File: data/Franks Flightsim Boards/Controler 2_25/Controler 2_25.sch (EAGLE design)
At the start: 16 parts, among them IC1 3_3V, IC2 5V, J3 External, J4 FEMALE 2x3

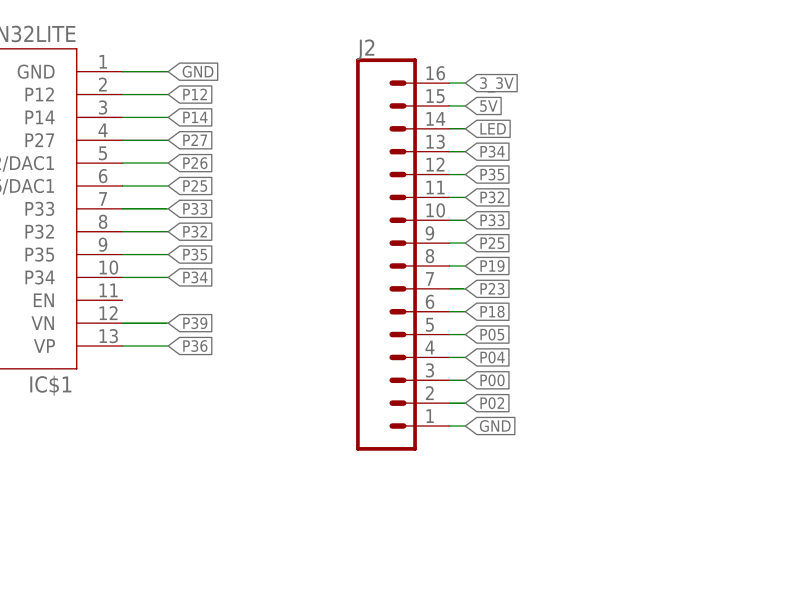
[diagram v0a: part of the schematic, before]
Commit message: new PCB
Updated with new pcb for 2_25 version
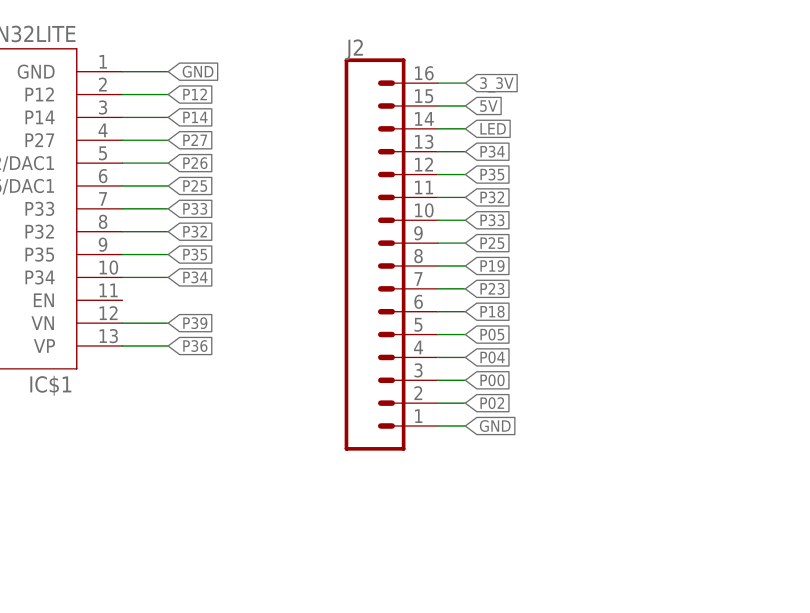
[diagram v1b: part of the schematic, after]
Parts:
- J2: device SparkFun-Connectors:CONN_16CENTER -> SparkFun-Connectors:CONN_16
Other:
- moved on the sheet: J2

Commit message: Update dev status
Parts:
- C1: device resistor:C-EUC0805 -> resistor:C-EUC1206
- C5: device resistor:CPOL-EU153CLV-0505 -> resistor:CPOL-EU153CLV-0605
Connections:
- net P12 renamed SRV1
- removed net P13: IC$1.P13/R14, J4.1
- removed net P15: IC$1.P15/R13, J4.2
- new net SRV2: IC$1.P15/R13, J4.1
- new net SRV3: IC$1.P13/R14, J4.2
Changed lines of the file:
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@@
 </class>
 <class number="1" name="GND" width="0.508" drill="0">
+<clearance class="1" value="0.254"/>
 </class>
 <class number="2" name="12V" width="0.762" drill="0">
@@
 <part name="IC2" library="SparkFun-IC-Power" library_urn="urn:adsk.eagle:library:526" deviceset="V_REG_LM1117" device="SOT223" package3d_urn="urn:adsk.eagle:package:39069/1" value="5V"/>
 <part name="C2" library="resistor" library_urn="urn:adsk.eagle:library:348" deviceset="CPOL-EU" device="CT3528" package3d_urn="urn:adsk.eagle:package:25815/1" value="47uF"/>
-<part name="C1" library="resistor" library_urn="urn:adsk.eagle:library:348" deviceset="C-EU" device="C0805" package3d_urn="urn:adsk.eagle:package:26137/1" value="100nF"/>
+<part name="C1" library="resistor" library_urn="urn:adsk.eagle:library:348" deviceset="C-EU" device="C1206" package3d_urn="urn:adsk.eagle:package:26140/1" value="100nF"/>
 <part name="C4" library="resistor" library_urn="urn:adsk.eagle:library:348" deviceset="CPOL-EU" device="CT3528" package3d_urn="urn:adsk.eagle:package:25815/1" value="47uF"/>
 <part name="C3" library="resistor" library_urn="urn:adsk.eagle:library:348" deviceset="C-EU" device="C0805" package3d_urn="urn:adsk.eagle:package:26137/1" value="100nF"/>
@@
 <part name="J1" library="SparkFun-Connectors" library_urn="urn:adsk.eagle:library:513" deviceset="CONN_03" device="" package3d_urn="urn:adsk.eagle:package:38063/1"/>
 <part name="J4" library="SparkFun-Connectors" library_urn="urn:adsk.eagle:library:513" deviceset="CONN_03X2" device="FEMALE" package3d_urn="urn:adsk.eagle:package:38016/1" value="FEMALE 2x3"/>
-<part name="C5" library="resistor" library_urn="urn:adsk.eagle:library:348" deviceset="CPOL-EU" device="153CLV-0505" package3d_urn="urn:adsk.eagle:package:25890/1" value="47uF"/>
+<part name="C5" library="resistor" library_urn="urn:adsk.eagle:library:348" deviceset="CPOL-EU" device="153CLV-0605" package3d_urn="urn:adsk.eagle:package:25889/1" value="47uF"/>
 <part name="C6" library="resistor" library_urn="urn:adsk.eagle:library:348" deviceset="C-EU" device="C0805" package3d_urn="urn:adsk.eagle:package:26137/1" value="100nF"/>
 </parts>
@@
 </segment>
 </net>
-<net name="P15" class="0">
+<net name="SRV3" class="0">
+<segment>
+<pinref part="IC$1" gate="G$1" pin="P13/R14"/>
+<wire x1="38.1" y1="106.68" x2="33.02" y2="106.68" width="0.1524" layer="91"/>
+<label x="33.02" y="106.68" size="1.27" layer="95" ratio="7" rot="R180" xref="yes"/>
+</segment>
+<segment>
+<pinref part="J4" gate="G$1" pin="2"/>
+<wire x1="7.62" y1="58.42" x2="10.16" y2="58.42" width="0.1524" layer="91"/>
+<label x="10.16" y="58.42" size="1.27" layer="95" xref="yes"/>
+</segment>
+</net>
+<net name="SRV2" class="0">
 <segment>
 <pinref part="IC$1" gate="G$1" pin="P15/R13"/>
@@
 </segment>
 <segment>
-<pinref part="J4" gate="G$1" pin="2"/>
-<wire x1="7.62" y1="58.42" x2="10.16" y2="58.42" width="0.1524" layer="91"/>
-<label x="10.16" y="58.42" size="1.27" layer="95" xref="yes"/>
-</segment>
-</net>
-<net name="P13" class="0">
-<segment>
-<pinref part="IC$1" gate="G$1" pin="P13/R14"/>
-<wire x1="38.1" y1="106.68" x2="33.02" y2="106.68" width="0.1524" layer="91"/>
-<label x="33.02" y="106.68" size="1.27" layer="95" ratio="7" rot="R180" xref="yes"/>
-</segment>
-<segment>
 <label x="-10.16" y="58.42" size="1.27" layer="95" rot="MR0" xref="yes"/>
 <pinref part="J4" gate="G$1" pin="1"/>
@@
 </segment>
 </net>
-<net name="P12" class="0">
+<net name="SRV1" class="0">
 <segment>
 <pinref part="IC$1" gate="G$1" pin="P12"/>

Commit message: update and backup
Update
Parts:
- C3, C6: device resistor:C-EUC0805 -> resistor:C-EUC1206
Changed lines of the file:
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@@
 <grid distance="0.1" unitdist="inch" unit="inch" style="lines" multiple="1" display="no" altdistance="0.01" altunitdist="inch" altunit="inch"/>
 <layers>
-<layer number="1" name="Top" color="4" fill="1" visible="no" active="no"/>
-<layer number="16" name="Bottom" color="1" fill="1" visible="no" active="no"/>
-<layer number="17" name="Pads" color="2" fill="1" visible="no" active="no"/>
-<layer number="18" name="Vias" color="2" fill="1" visible="no" active="no"/>
-<layer number="19" name="Unrouted" color="6" fill="1" visible="no" active="no"/>
-<layer number="20" name="Dimension" color="24" fill="1" visible="no" active="no"/>
-<layer number="21" name="tPlace" color="7" fill="1" visible="no" active="no"/>
-<layer number="22" name="bPlace" color="7" fill="1" visible="no" active="no"/>
-<layer number="23" name="tOrigins" color="15" fill="1" visible="no" active="no"/>
-<layer number="24" name="bOrigins" color="15" fill="1" visible="no" active="no"/>
-<layer number="25" name="tNames" color="7" fill="1" visible="no" active="no"/>
-<layer number="26" name="bNames" color="7" fill="1" visible="no" active="no"/>
-<layer number="27" name="tValues" color="7" fill="1" visible="no" active="no"/>
-<layer number="28" name="bValues" color="7" fill="1" visible="no" active="no"/>
+<layer number="1" name="Top" color="4" fill="1" visible="yes" active="no"/>
+<layer number="16" name="Bottom" color="1" fill="1" visible="yes" active="no"/>
+<layer number="17" name="Pads" color="2" fill="1" visible="yes" active="no"/>
+<layer number="18" name="Vias" color="2" fill="1" visible="yes" active="no"/>
+<layer number="19" name="Unrouted" color="6" fill="1" visible="yes" active="no"/>
+<layer number="20" name="Dimension" color="24" fill="1" visible="yes" active="no"/>
+<layer number="21" name="tPlace" color="7" fill="1" visible="yes" active="no"/>
+<layer number="22" name="bPlace" color="7" fill="1" visible="yes" active="no"/>
+<layer number="23" name="tOrigins" color="15" fill="1" visible="yes" active="no"/>
+<layer number="24" name="bOrigins" color="15" fill="1" visible="yes" active="no"/>
+<layer number="25" name="tNames" color="7" fill="1" visible="yes" active="no"/>
+<layer number="26" name="bNames" color="7" fill="1" visible="yes" active="no"/>
+<layer number="27" name="tValues" color="7" fill="1" visible="yes" active="no"/>
+<layer number="28" name="bValues" color="7" fill="1" visible="yes" active="no"/>
 <layer number="29" name="tStop" color="7" fill="3" visible="no" active="no"/>
 <layer number="30" name="bStop" color="7" fill="6" visible="no" active="no"/>
@@
 <layer number="35" name="tGlue" color="7" fill="4" visible="no" active="no"/>
 <layer number="36" name="bGlue" color="7" fill="5" visible="no" active="no"/>
-<layer number="37" name="tTest" color="7" fill="1" visible="no" active="no"/>
-<layer number="38" name="bTest" color="7" fill="1" visible="no" active="no"/>
+<layer number="37" name="tTest" color="7" fill="1" visible="yes" active="no"/>
+<layer number="38" name="bTest" color="7" fill="1" visible="yes" active="no"/>
 <layer number="39" name="tKeepout" color="4" fill="11" visible="no" active="no"/>
 <layer number="40" name="bKeepout" color="1" fill="11" visible="no" active="no"/>
@@
 <layer number="44" name="Drills" color="7" fill="1" visible="no" active="no"/>
 <layer number="45" name="Holes" color="7" fill="1" visible="no" active="no"/>
-<layer number="46" name="Milling" color="3" fill="1" visible="no" active="no"/>
-<layer number="47" name="Measures" color="7" fill="1" visible="no" active="no"/>
-<layer number="48" name="Document" color="7" fill="1" visible="no" active="no"/>
-<layer number="49" name="Reference" color="7" fill="1" visible="no" active="no"/>
-<layer number="50" name="dxf" color="7" fill="1" visible="no" active="no"/>
-<layer number="51" name="tDocu" color="7" fill="1" visible="no" active="no"/>
-<layer number="52" name="bDocu" color="7" fill="1" visible="no" active="no"/>
-<layer number="53" name="tGND_GNDA" color="7" fill="9" visible="no" active="no"/>
-<layer number="54" name="bGND_GNDA" color="1" fill="9" visible="no" active="no"/>
-<layer number="56" name="wert" color="7" fill="1" visible="no" active="no"/>
-<layer number="57" name="tCAD" color="7" fill="1" visible="no" active="no"/>
-<layer number="59" name="tCarbon" color="7" fill="1" visible="no" active="no"/>
-<layer number="60" name="bCarbon" color="7" fill="1" visible="no" active="no"/>
+<layer number="46" name="Milling" color="3" fill="1" visible="yes" active="no"/>
+<layer number="47" name="Measures" color="7" fill="1" visible="yes" active="no"/>
+<layer number="48" name="Document" color="7" fill="1" visible="yes" active="no"/>
+<layer number="49" name="Reference" color="7" fill="1" visible="yes" active="no"/>
+<layer number="50" name="dxf" color="7" fill="1" visible="yes" active="no"/>
+<layer number="51" name="tDocu" color="7" fill="1" visible="yes" active="no"/>
+<layer number="52" name="bDocu" color="7" fill="1" visible="yes" active="no"/>
+<layer number="53" name="tGND_GNDA" color="7" fill="9" visible="yes" active="no"/>
+<layer number="54" name="bGND_GNDA" color="1" fill="9" visible="yes" active="no"/>
+<layer number="56" name="wert" color="7" fill="1" visible="yes" active="no"/>
+<layer number="57" name="tCAD" color="7" fill="1" visible="yes" active="no"/>
+<layer number="59" name="tCarbon" color="7" fill="1" visible="yes" active="no"/>
+<layer number="60" name="bCarbon" color="7" fill="1" visible="yes" active="no"/>
 <layer number="88" name="SimResults" color="9" fill="1" visible="yes" active="yes"/>
 <layer number="89" name="SimProbes" color="9" fill="1" visible="yes" active="yes"/>
@@
 <part name="C1" library="resistor" library_urn="urn:adsk.eagle:library:348" deviceset="C-EU" device="C1206" package3d_urn="urn:adsk.eagle:package:26140/1" value="100nF"/>
 <part name="C4" library="resistor" library_urn="urn:adsk.eagle:library:348" deviceset="CPOL-EU" device="CT3528" package3d_urn="urn:adsk.eagle:package:25815/1" value="47uF"/>
-<part name="C3" library="resistor" library_urn="urn:adsk.eagle:library:348" deviceset="C-EU" device="C0805" package3d_urn="urn:adsk.eagle:package:26137/1" value="100nF"/>
+<part name="C3" library="resistor" library_urn="urn:adsk.eagle:library:348" deviceset="C-EU" device="C1206" package3d_urn="urn:adsk.eagle:package:26140/1" value="100nF"/>
 <part name="J2" library="SparkFun-Connectors" library_urn="urn:adsk.eagle:library:513" deviceset="CONN_16" device="" package3d_urn="urn:adsk.eagle:package:38258/1"/>
 <part name="J3" library="con-molex" library_urn="urn:adsk.eagle:library:165" deviceset="22-?-05" device="27-2051" value="External"/>
@@
 <part name="J4" library="SparkFun-Connectors" library_urn="urn:adsk.eagle:library:513" deviceset="CONN_03X2" device="FEMALE" package3d_urn="urn:adsk.eagle:package:38016/1" value="FEMALE 2x3"/>
 <part name="C5" library="resistor" library_urn="urn:adsk.eagle:library:348" deviceset="CPOL-EU" device="153CLV-0605" package3d_urn="urn:adsk.eagle:package:25889/1" value="47uF"/>
-<part name="C6" library="resistor" library_urn="urn:adsk.eagle:library:348" deviceset="C-EU" device="C0805" package3d_urn="urn:adsk.eagle:package:26137/1" value="100nF"/>
+<part name="C6" library="resistor" library_urn="urn:adsk.eagle:library:348" deviceset="C-EU" device="C1206" package3d_urn="urn:adsk.eagle:package:26140/1" value="100nF"/>
 </parts>
 <sheets>
